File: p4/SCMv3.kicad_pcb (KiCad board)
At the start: 2 copper layers, 58.7 x 110.9 mm, 127 parts, among them IC1 40106, IC2 40106, IC3 TL082, J1 Conn_01x06, J1-OUT8 JACK-MONO-SWB, J2 Conn_01x02, J2-OUT7 JACK-MONO-SWB, J3 POWER, J3-OUT6 JACK-MONO-SWB, J4 Conn_01x02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

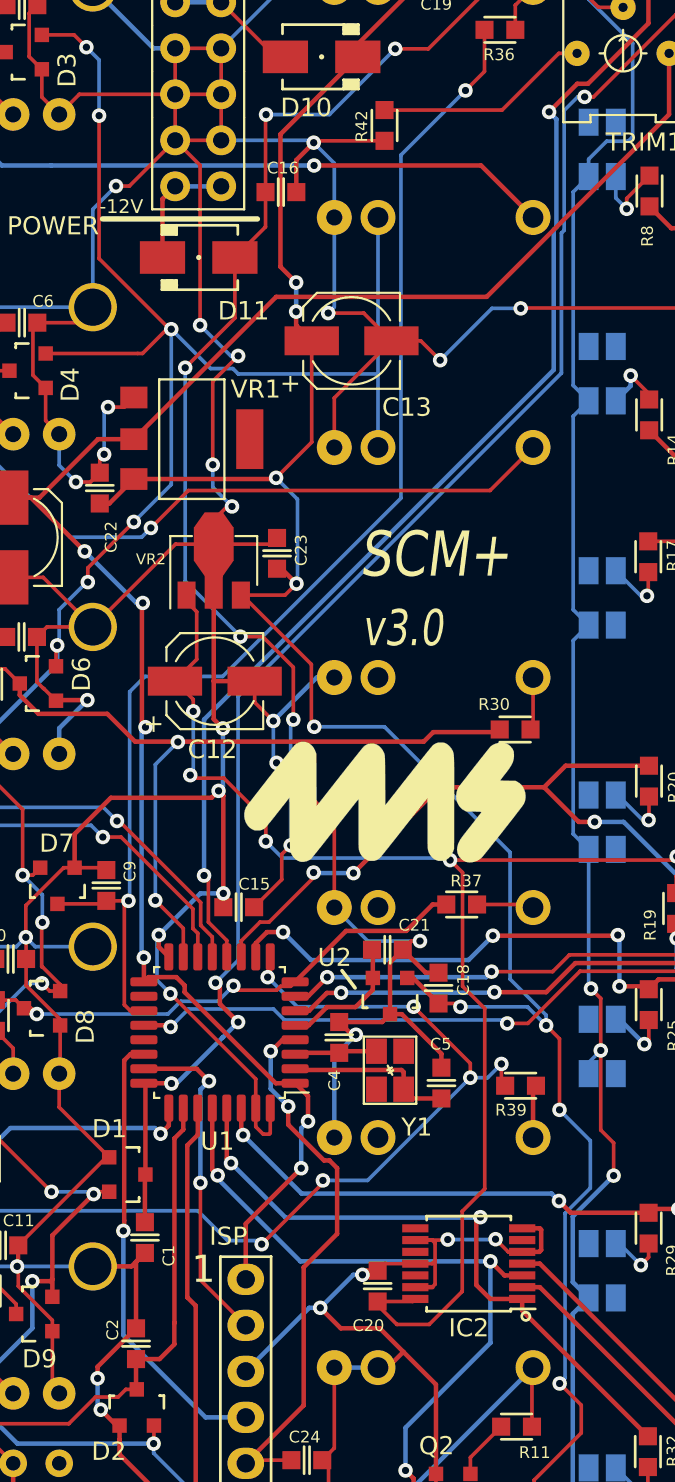
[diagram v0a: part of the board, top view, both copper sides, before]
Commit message: Applied routing changes to p4 PCB
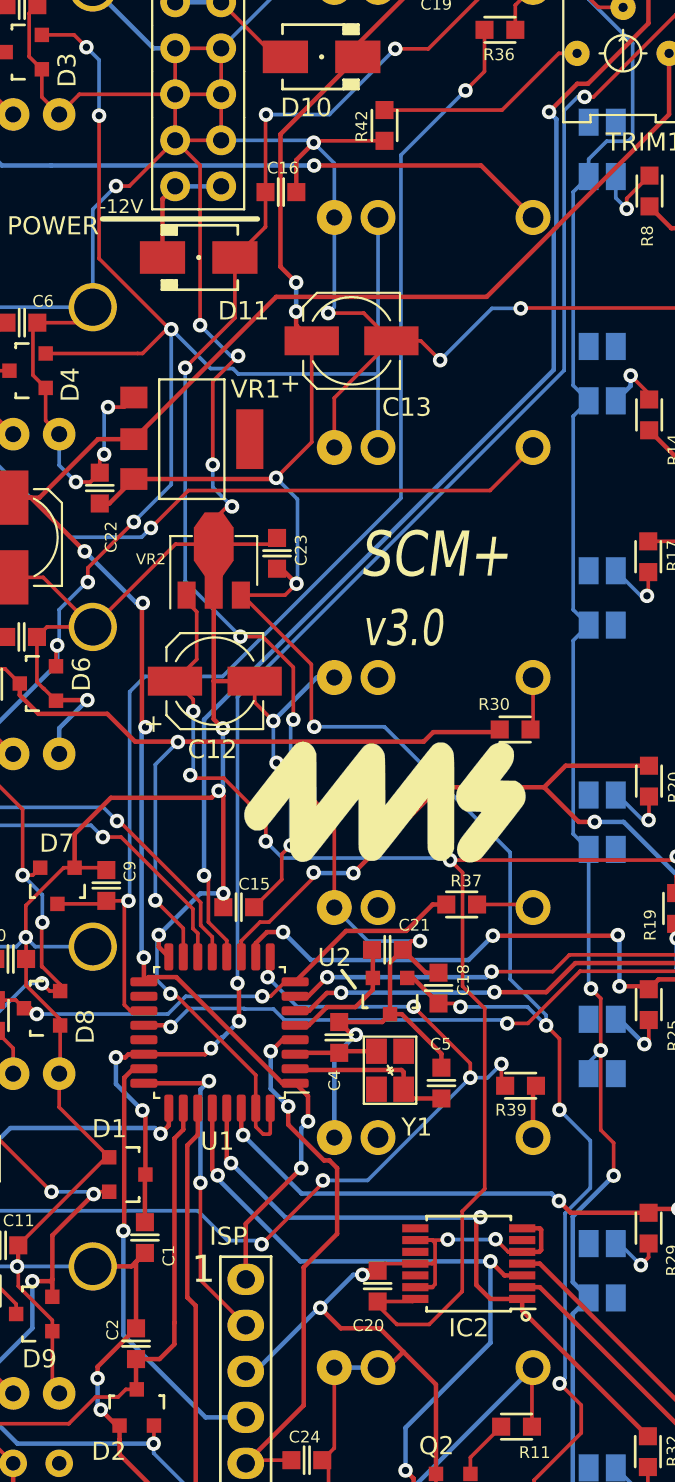
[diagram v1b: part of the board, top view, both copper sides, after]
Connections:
- U1 pad 22: /SWDIO -> /UC_CLK_IN
- U1 pad 23: /SWCLK -> /SWDIO
- U1 pad 24: /UC_CLK_IN -> /SWCLK
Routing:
- net /UC_CLK_IN: track 85.6 -> 87.6 mm, vias 4 -> 6
- net /SWDIO: track 25.1 -> 24.2 mm

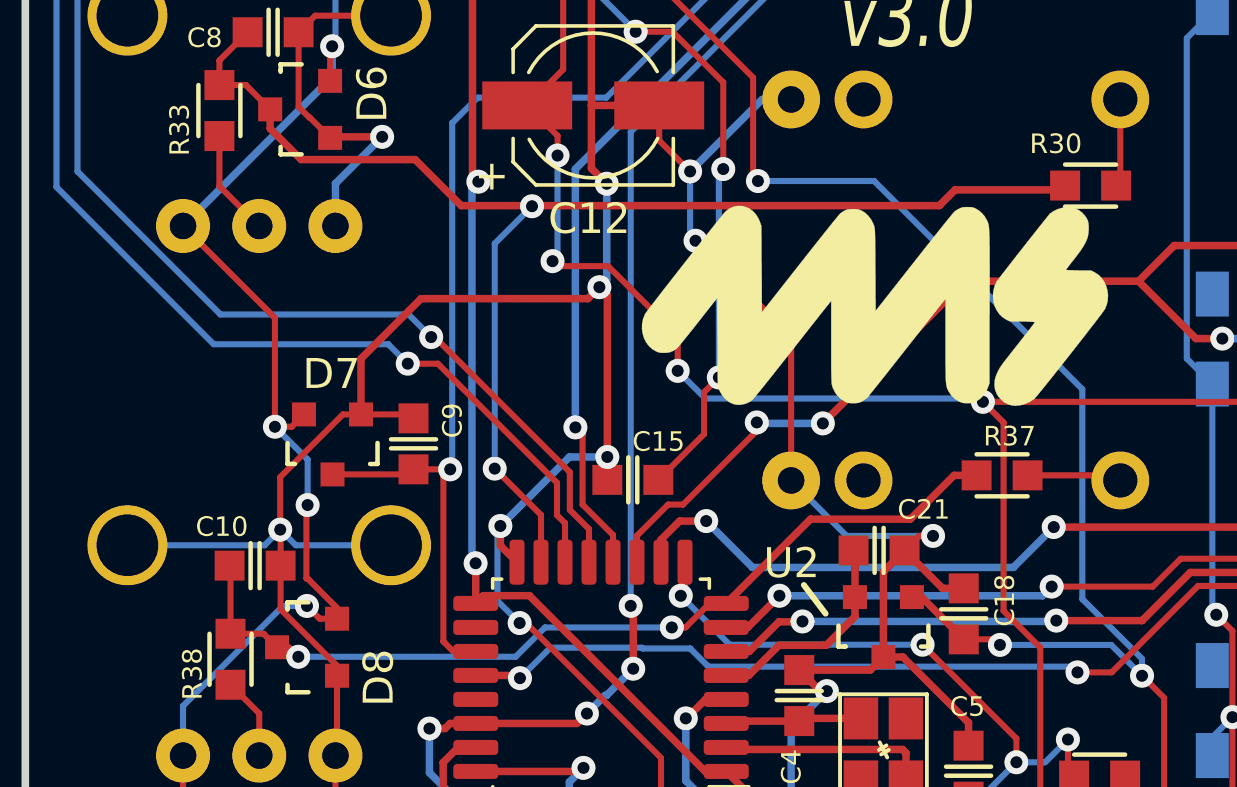
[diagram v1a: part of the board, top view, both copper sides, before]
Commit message: changed +5V net over to +3.3VA
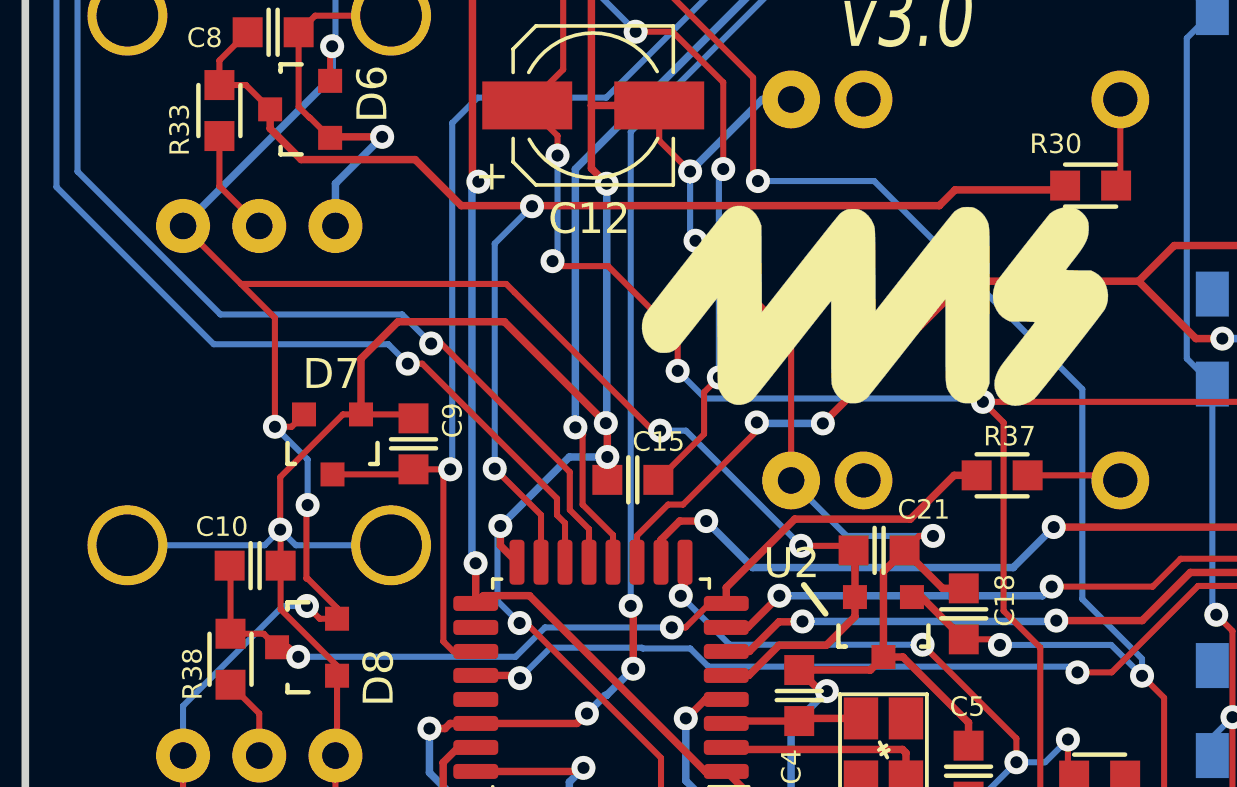
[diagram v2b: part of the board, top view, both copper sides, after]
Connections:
- D1 pad 2: +5V -> +3.3VA
- D2 pad 2: +5V -> +3.3VA
- D3 pad 2: +5V -> +3.3VA
- D4 pad 2: +5V -> +3.3VA
- D5 pad 2: +5V -> +3.3VA
- D6 pad 2: +5V -> +3.3VA
- D7 pad 2: +5V -> +3.3VA
- D8 pad 2: +5V -> +3.3VA
- D9 pad 2: +5V -> +3.3VA
- JROTATE1 pad 3: +5V -> +3.3VA
- JSLIP1 pad 3: +5V -> +3.3VA
- PPW1 pad 3: +5V -> +3.3VA
- PSHUFFLE1 pad 3: +5V -> +3.3VA
- PSKIP1 pad 3: +5V -> +3.3VA
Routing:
- net +3.3VA: track 7.33 -> 187.1 mm, vias 0 -> 16
- net +5V: track 155.7 -> 0.00 mm, vias 14 -> 0
- net GND: track 633.3 -> 634.3 mm

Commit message: WIP updating p4
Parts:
- removed IC1, IC2: 40106, 4ms_Package_SSOP:TSSOP-14_4.4x5mm_P0.65mm
- removed VR2: UA78L08, 4ms_Package_SOT:SOT89-3
- added U3: CD40109BPWR, Package_SO:TSSOP-16_4.4x5mm_P0.65mm, F.Cu at (76.7, 36.3)
- added U4: CD40109BPWR, Package_SO:TSSOP-16_4.4x5mm_P0.65mm, F.Cu at (85.5, 36.3)
- C12: value 47uF_5x5.3_16V -> 0.1uF_0603_16V; footprint 4ms_Capacitor:CP_Elec_5x5.3 -> 4ms_Capacitor:C_0603
- J1-OUT8, J2-OUT7, J3-OUT6, J4-OUT5, J5-OUT4, J6-OUT3, J7-OUT2, J8-OUT1: value JACK-MONO-SWB -> 3.5mm_Mono_Switched_SymSmall_0.05
- J3: value POWER -> Conn_02x08
- J9-CLK_IN1: value JCLK_IN -> 3.5mm_Mono_Switched_SymSmall_0.05
- JFAST1, JMUTE1: value 3.5mm_Stereo_SymSmall_0.05 -> 3.5mm_Mono_Switched_SymSmall_0.05
- JPW1: value JPW -> 3.5mm_Mono_Switched_SymSmall_0.05
- JRESYNC1: value JRESYNC -> 3.5mm_Mono_Switched_SymSmall_0.05
- JROTATE1: value JROTATE -> 3.5mm_Mono_Switched_SymSmall_0.05
- JSHUFFLE1: value JSHUFFLE -> 3.5mm_Mono_Switched_SymSmall_0.05
- JSKIP1: value JSKIP -> 3.5mm_Mono_Switched_SymSmall_0.05
- JSLIP1: value JSLIP -> 3.5mm_Mono_Switched_SymSmall_0.05
- LED1, LED7, LED8: value BLUE -> RGB_CA_PLCC4
- LED2, LED3, LED4, LED5, LED6: value GREEN -> RGB_CA_PLCC4
- LED9: value WHITE -> RGB_CA_PLCC4
- R10, R13, R21, R22, R27, R3, R36, R7: value 470R_0805_350mW -> 470R_0603
- VR1: value LD1117S33 -> LD1117-3.3V-SOT223
- moved C15 39.5 mm to (22.6, 20.4), turned to 0 degrees
- moved C16 21.2 mm to (35.2, 3.32), turned to 180 degrees
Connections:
- C12 pad 1: +8V -> +3V3
- C17 pad 1: +8V -> +3V3
- C20 pad 1: +8V -> +12V
- D1 pad 2: +3.3VA -> +3V3
- D3 pad 2: +3.3VA -> +3V3
- D4 pad 2: +3.3VA -> +3V3
- D5 pad 2: +3.3VA -> +3V3
- D6 pad 2: +3.3VA -> +3V3
- D7 pad 2: +3.3VA -> +3V3
- D8 pad 2: +3.3VA -> +3V3
- D9 pad 2: +3.3VA -> +3V3
- IC3 pad 1: /VREF -> /VLEDSINK
- IC3 pad 2: /VREF -> /VLEDSINK
- LED1 pad 2: /VREF -> /UC_OUT8
- LED2 pad 2: /VREF -> /UC_OUT7
- LED3 pad 2: /VREF -> /UC_OUT6
- LED4 pad 2: /VREF -> /UC_OUT5
- LED5 pad 2: /VREF -> /UC_OUT4
- LED6 pad 2: /VREF -> /UC_OUT3
- LED7 pad 2: /VREF -> /UC_OUT2
- LED8 pad 2: /VREF -> /UC_OUT1
- LED9 pad 2: /VREF -> /UC_LED_IN
- R1 pad 1: /UC_LED_IN -> /VLEDSINK
- R14 pad 1: /UC_OUT2 -> /VLEDSINK
- R17 pad 1: /UC_OUT3 -> /VLEDSINK
- R2 pad 1: /UC_LED_IN -> /VLEDSINK
- R20 pad 1: /UC_OUT4 -> /VLEDSINK
- R25 pad 1: /UC_OUT5 -> /VLEDSINK
- R29 pad 1: /UC_OUT6 -> /VLEDSINK
- R32 pad 1: /UC_OUT7 -> /VLEDSINK
- R35 pad 1: /UC_OUT8 -> /VLEDSINK
- R4 pad 1: /UC_LED_IN -> /VLEDSINK
- R42 pad 1: Net-(R42-Pad1) -> +3V3
- R42 pad 2: GND -> Net-(R42-Pad2)
- R8 pad 1: /UC_OUT1 -> /VLEDSINK
- TRIM1 pad 1: Net-(R42-Pad1) -> GND
- TRIM1 pad 3: +3V3 -> Net-(R42-Pad2)
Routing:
- net /VLEDSINK: track 0.00 -> 335.7 mm, vias 0 -> 17
- net /VREF: track 115.5 -> 0.00 mm, vias 4 -> 0
- net +3V3: track 102.4 -> 207.7 mm, vias 6 -> 12
- net +8V: track 93.0 -> 0.00 mm, vias 6 -> 0
- net /UC_LED_IN: track 78.8 -> 0.00 mm, vias 2 -> 0
- net /UC_OUT8: track 62.9 -> 0.00 mm, vias 5 -> 0
- net /UC_OUT6: track 43.2 -> 0.00 mm, vias 4 -> 0
- net -12VA: track 70.0 -> 30.8 mm, vias 6 -> 2
- net /UC_OUT7: track 35.3 -> 0.00 mm, vias 2 -> 0
- net Net-(R42-Pad1): track 12.3 -> 0.00 mm
- net GND: track 634.3 -> 639.3 mm
